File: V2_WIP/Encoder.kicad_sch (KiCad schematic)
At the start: 8 parts, among them SW701 RotaryEncoder

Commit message: fixed errors in schematic
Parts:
- R_E701, R_E702, R_E703, R_E704: footprint Resistor_SMD:R_0805_2012Metric_Pad1.20x1.40mm_HandSolder -> Resistor_SMD:R_0603_1608Metric_Pad0.98x0.95mm_HandSolder
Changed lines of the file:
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@@
 			)
 		)
-		(property "Footprint" "Resistor_SMD:R_0805_2012Metric_Pad1.20x1.40mm_HandSolder"
+		(property "Footprint" "Resistor_SMD:R_0603_1608Metric_Pad0.98x0.95mm_HandSolder"
 			(at 157.988 80.01 90)
 			(effects
@@
 			)
 		)
-		(property "Footprint" "Resistor_SMD:R_0805_2012Metric_Pad1.20x1.40mm_HandSolder"
+		(property "Footprint" "Resistor_SMD:R_0603_1608Metric_Pad0.98x0.95mm_HandSolder"
 			(at 161.29 88.138 90)
 			(effects
@@
 			)
 		)
-		(property "Footprint" "Resistor_SMD:R_0805_2012Metric_Pad1.20x1.40mm_HandSolder"
+		(property "Footprint" "Resistor_SMD:R_0603_1608Metric_Pad0.98x0.95mm_HandSolder"
 			(at 135.128 82.55 90)
 			(effects
@@
 			)
 		)
-		(property "Footprint" "Resistor_SMD:R_0805_2012Metric_Pad1.20x1.40mm_HandSolder"
+		(property "Footprint" "Resistor_SMD:R_0603_1608Metric_Pad0.98x0.95mm_HandSolder"
 			(at 131.572 95.25 90)
 			(effects

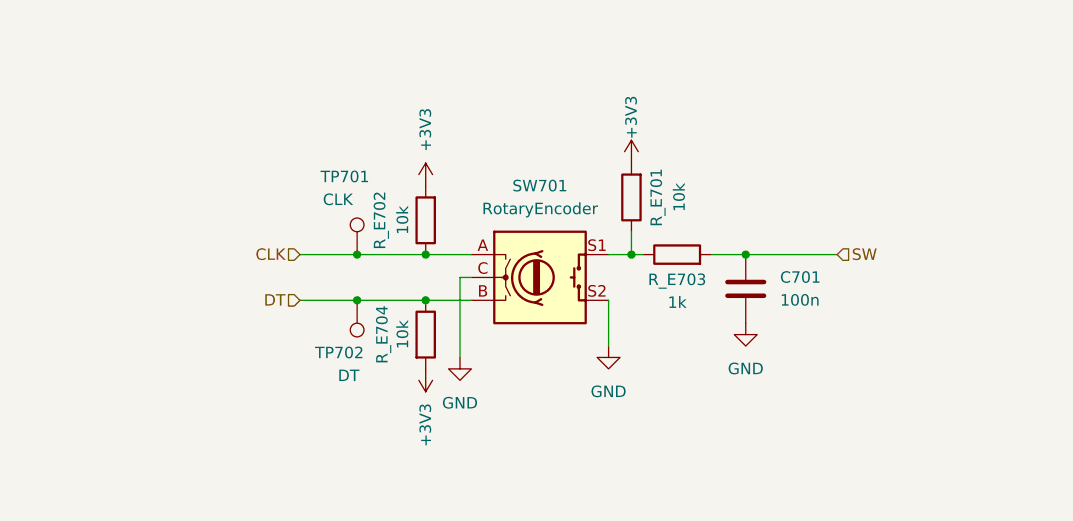
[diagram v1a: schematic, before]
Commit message: Removed EEPROM, Adjusted Flash connection, renamed ESP pins and several other signals
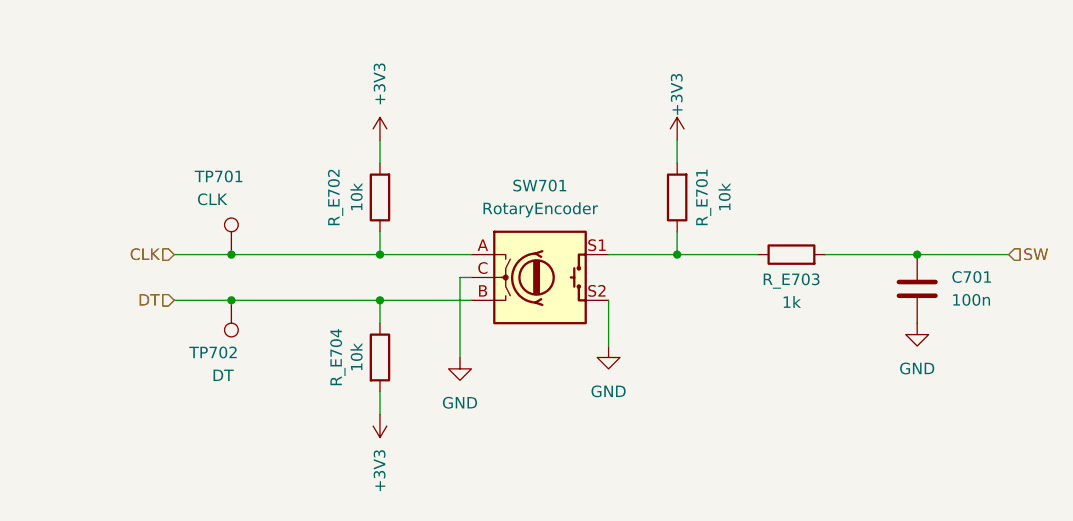
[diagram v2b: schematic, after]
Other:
- moved on the sheet: C701, R_E701, R_E702, R_E703, R_E704, TP701, TP702

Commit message: finallizes schematic; pcb progress
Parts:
- added C702, C703: 1n, Capacitor_SMD:C_0603_1608Metric_Pad1.08x0.95mm_HandSolder, symbol Device:C
- added R_E705, R_E706: 47, Resistor_SMD:R_0603_1608Metric_Pad0.98x0.95mm_HandSolder, symbol Device:R
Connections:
- net CLK: now also C703.1, R_E705.1; no longer SW701.A
- net DT: now also C702.1, R_E706.1; no longer SW701.B
- net GND: now also C702.2, C703.2
- new net: R_E705.2, SW701.A
- new net: R_E706.2, SW701.B
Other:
- moved on the sheet: R_E702, TP701, TP702

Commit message: updated most datashets
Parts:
- C701: value 100n -> 100nF
- C702, C703: value 1n -> 1nF
- R_E703: value 1k -> 2k
- SW701: value RotaryEncoder -> *RotaryEncoder
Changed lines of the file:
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@@
 			)
 		)
-		(property "Datasheet" "~"
+		(property "Datasheet" "https://cz.mouser.com/ProductDetail/SEI-Stackpole/RNCE0603BTE10K0?qs=sGAEpiMZZMtlubZbdhIBIGfmJML7fLMVDBbNntjsT8g%3D"
 			(at 161.29 80.01 0)
 			(effects
@@
 			)
 		)
+		(property "Purchase-URL" ""
+			(at 161.29 80.01 0)
+			(effects
+				(font
+					(size 1.27 1.27)
+				)
+				(hide yes)
+			)
+		)
 		(pin "1"
 		)
@@
 			)
 		)
-		(property "Value" "1k"
+		(property "Value" "2k"
 			(at 173.99 91.694 90)
 			(effects
@@
 			)
 		)
-		(property "Datasheet" "~"
+		(property "Datasheet" "https://cz.mouser.com/ProductDetail/SEI-Stackpole/RNCE0603BTE2K00?qs=sGAEpiMZZMtlubZbdhIBIGfmJML7fLMVr3bVQ0UuJPQ%3D"
 			(at 173.99 86.36 0)
 			(effects
@@
 			)
 		)
+		(property "Purchase-URL" ""
+			(at 173.99 86.36 0)
+			(effects
+				(font
+					(size 1.27 1.27)
+				)
+				(hide yes)
+			)
+		)
 		(pin "1"
 		)
@@
 			)
 		)
+		(property "Purchase-URL" ""
+			(at 96.52 80.01 0)
+			(effects
+				(font
+					(size 1.27 1.27)
+				)
+				(hide yes)
+			)
+		)
 		(pin "1"
 		)
@@
 			)
 		)
-		(property "Value" "1n"
+		(property "Value" "1nF"
 			(at 118.364 102.87 0)
 			(effects
@@
 			)
 		)
-		(property "Datasheet" "~"
+		(property "Datasheet" "https://cz.mouser.com/ProductDetail/KYOCERA-AVX/06031A102JAT2A?qs=%252BdQmOuGyFcGHJqs3Zmdykg%3D%3D"
 			(at 115.57 101.6 0)
 			(effects
@@
 		)
 		(property "Description" "Unpolarized capacitor"
+			(at 115.57 101.6 0)
+			(effects
+				(font
+					(size 1.27 1.27)
+				)
+				(hide yes)
+			)
+		)
+		(property "Purchase-URL" ""
 			(at 115.57 101.6 0)
 			(effects
@@
 			)
 		)
-		(property "Value" "RotaryEncoder"
+		(property "Value" "*RotaryEncoder"
 			(at 146.05 81.28 0)
 			(effects
@@
 			)
 		)
+		(property "Purchase-URL" ""
+			(at 146.05 88.9 0)
+			(effects
+				(font
+					(size 1.27 1.27)
+				)
+				(hide yes)
+			)
+		)
 		(pin "A"
 		)
@@
 			)
 		)
-		(property "Datasheet" "~"
+		(property "Datasheet" "https://cz.mouser.com/ProductDetail/Vishay-Beyschlag/MCT06030D4709BP500?qs=sGAEpiMZZMtlubZbdhIBIOF8iwLVxXp6Oa2rPEx3MVU%3D"
 			(at 129.54 80.01 0)
 			(effects
@@
 			)
 		)
+		(property "Purchase-URL" ""
+			(at 129.54 80.01 0)
+			(effects
+				(font
+					(size 1.27 1.27)
+				)
+				(hide yes)
+			)
+		)
 		(pin "1"
 		)
@@
 			)
 		)
+		(property "Purchase-URL" ""
+			(at 96.52 97.79 0)
+			(effects
+				(font
+					(size 1.27 1.27)
+				)
+				(hide yes)
+			)
+		)
 		(pin "1"
 		)
@@
 			)
 		)
-		(property "Datasheet" "~"
+		(property "Datasheet" "https://cz.mouser.com/ProductDetail/SEI-Stackpole/RNCE0603BTE10K0?qs=sGAEpiMZZMtlubZbdhIBIGfmJML7fLMVDBbNntjsT8g%3D"
 			(at 106.68 93.98 0)
 			(effects
@@
 			)
 		)
+		(property "Purchase-URL" ""
+			(at 106.68 93.98 0)
+			(effects
+				(font
+					(size 1.27 1.27)
+				)
+				(hide yes)
+			)
+		)
 		(pin "1"
 		)
@@
 			)
 		)
-		(property "Value" "1n"
+		(property "Value" "1nF"
 			(at 118.872 85.09 0)
 			(effects
@@
 			)
 		)
-		(property "Datasheet" "~"
+		(property "Datasheet" "https://cz.mouser.com/ProductDetail/KYOCERA-AVX/06031A102JAT2A?qs=%252BdQmOuGyFcGHJqs3Zmdykg%3D%3D"
 			(at 115.57 83.82 0)
 			(effects
@@
 		)
 		(property "Description" "Unpolarized capacitor"
+			(at 115.57 83.82 0)
+			(effects
+				(font
+					(size 1.27 1.27)
+				)
+				(hide yes)
+			)
+		)
+		(property "Purchase-URL" ""
 			(at 115.57 83.82 0)
 			(effects
@@
 			)
 		)
-		(property "Datasheet" "~"
+		(property "Datasheet" "https://cz.mouser.com/ProductDetail/SEI-Stackpole/RNCE0603BTE10K0?qs=sGAEpiMZZMtlubZbdhIBIGfmJML7fLMVDBbNntjsT8g%3D"
 			(at 106.68 73.66 0)
 			(effects
@@
 			)
 		)
+		(property "Purchase-URL" ""
+			(at 106.68 73.66 0)
+			(effects
+				(font
+					(size 1.27 1.27)
+				)
+				(hide yes)
+			)
+		)
 		(pin "1"
 		)
@@
 			)
 		)
-		(property "Datasheet" "~"
+		(property "Datasheet" "https://cz.mouser.com/ProductDetail/Vishay-Beyschlag/MCT06030D4709BP500?qs=sGAEpiMZZMtlubZbdhIBIOF8iwLVxXp6Oa2rPEx3MVU%3D"
 			(at 129.54 97.79 0)
 			(effects
@@
 		)
 		(property "Description" "Resistor"
+			(at 129.54 97.79 0)
+			(effects
+				(font
+					(size 1.27 1.27)
+				)
+				(hide yes)
+			)
+		)
+		(property "Purchase-URL" ""
 			(at 129.54 97.79 0)
 			(effects
@@
 			)
 		)
-		(property "Value" "100n"
+		(property "Value" "100nF"
 			(at 191.77 91.4399 0)
 			(effects
@@
 			)
 		)
-		(property "Datasheet" "~"
+		(property "Datasheet" "https://cz.mouser.com/ProductDetail/KYOCERA-AVX/0603ZG104ZAT2A?qs=XWDBCzcA0Tke70DI9cEVbA%3D%3D"
 			(at 187.96 90.17 0)
 			(effects
@@
 			(at 187.96 90.17 0)
 			(effects
+				(font
+					(size 1.27 1.27)
+				)
+				(hide yes)
+			)
+		)
+		(property "Purchase-URL" ""
+			(at 187.96 90.17 0)
+			(effects

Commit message: up to date i dont remember what changed
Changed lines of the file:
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@@
 (kicad_sch
-	(version 20231120)
+	(version 20250114)
 	(generator "eeschema")
-	(generator_version "8.0")
+	(generator_version "9.0")
 	(paper "A4")
 	(junction
@@
 		(shape input)
 		(at 93.98 97.79 180)
-		(fields_autoplaced yes)
 		(effects
 			(font
@@
 		(shape input)
 		(at 93.98 80.01 180)
-		(fields_autoplaced yes)
 		(effects
 			(font
@@
 		(shape input)
 		(at 198.12 86.36 0)
-		(fields_autoplaced yes)
 		(effects
 			(font
